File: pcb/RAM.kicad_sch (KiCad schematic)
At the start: 29 parts, among them U2 MT41K64M16TW-x

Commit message: Fix some symbols
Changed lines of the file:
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@@
   )
   (bus_alias "DQ_{L}" (members "DQ0" "DQ1" "DQ2" "DQ3" "DQ4" "DQ5" "DQ6" "DQ7" "LDM" "LDQS+" "LDQS-"))
-  (bus_alias "RAMCTRL" (members "ODT" "CKE" "CK+" "CK-" "~{MEM_RESET}" "~{CS}" "~{CAS}" "~{RAS}" "~{WE}"))
   (bus_alias "DQ_{U}" (members "DQ8" "DQ9" "DQ10" "DQ11" "DQ12" "DQ13" "DQ14" "DQ15" "UDM" "UDQS+" "UDQS-"))
   (bus_alias "RAMADDR" (members "A0" "A1" "A2" "A3" "A4" "A5" "A6" "A7" "A8" "A9" "A10" "A11" "A12" "BA0" "BA1" "BA2"))
+  (bus_alias "RAMCTRL" (members "ODT" "CKE" "CK+" "CK-" "~{MEM_RESET}" "~{CS}" "~{CAS}" "~{RAS}" "~{WE}"))
   (junction (at 158.75 38.1) (diameter 0) (color 0 0 0 0)
   )
@@
     (pin "2")
   )
-  (symbol (lib_name "RAM_VDD_2") (lib_id "ecp5u85-bse-usb:RAM_VDD") (at 86.36 24.13 0) (unit 1)
+  (symbol (lib_id "ecp5u85-bse-usb:RAM_VDD") (at 86.36 24.13 0) (unit 1)
     (in_bom yes) (on_board yes) (fields_autoplaced)
     (property "Reference" "#PWR0116" (id 0) (at 86.36 27.94 0)
@@
     (pin "1")
   )
+  (symbol (lib_id "power:PWR_FLAG") (at 144.78 27.94 0) (unit 1)
+    (in_bom yes) (on_board yes) (fields_autoplaced)
+    (property "Reference" "#FLG0102" (id 0) (at 144.78 26.035 0)
+      (effects (font (size 1.27 1.27)) hide)
+    )
+    (property "Value" "PWR_FLAG" (id 1) (at 144.78 22.86 0))
+    (property "Footprint" "" (id 2) (at 144.78 27.94 0)
+      (effects (font (size 1.27 1.27)) hide)
+    )
+    (property "Datasheet" "~" (id 3) (at 144.78 27.94 0)
+      (effects (font (size 1.27 1.27)) hide)
+    )
+    (pin "1")
+  )
   (symbol (lib_id "power:GND") (at 217.17 50.8 0) (mirror y) (unit 1)
     (in_bom yes) (on_board yes) (fields_autoplaced)
@@
     (pin "2")
   )
-  (symbol (lib_name "RAM_VDD_1") (lib_id "ecp5u85-bse-usb:RAM_VDD") (at 234.95 29.21 0) (unit 1)
+  (symbol (lib_id "ecp5u85-bse-usb:RAM_VDD") (at 234.95 29.21 0) (unit 1)
     (in_bom yes) (on_board yes) (fields_autoplaced)
     (property "Reference" "#PWR0112" (id 0) (at 234.95 33.02 0)
@@
     (pin "2")
   )
+  (symbol (lib_id "power:PWR_FLAG") (at 99.06 27.94 0) (unit 1)
+    (in_bom yes) (on_board yes) (fields_autoplaced)
+    (property "Reference" "#FLG0101" (id 0) (at 99.06 26.035 0)
+      (effects (font (size 1.27 1.27)) hide)
+    )
+    (property "Value" "PWR_FLAG" (id 1) (at 99.06 22.86 0))
+    (property "Footprint" "" (id 2) (at 99.06 27.94 0)
+      (effects (font (size 1.27 1.27)) hide)
+    )
+    (property "Datasheet" "~" (id 3) (at 99.06 27.94 0)
+      (effects (font (size 1.27 1.27)) hide)
+    )
+    (pin "1")
+  )
   (symbol (lib_id "Device:C") (at 73.66 44.45 0) (unit 1)

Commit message: Some extra fixes and notes
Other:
- note added: "We might need care with these chokes RAM can require 200-300mA at some moments"
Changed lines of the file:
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@@
   )
   (bus_alias "DQ_{L}" (members "DQ0" "DQ1" "DQ2" "DQ3" "DQ4" "DQ5" "DQ6" "DQ7" "LDM" "LDQS+" "LDQS-"))
+  (bus_alias "RAMADDR" (members "A0" "A1" "A2" "A3" "A4" "A5" "A6" "A7" "A8" "A9" "A10" "A11" "A12" "BA0" "BA1" "BA2"))
   (bus_alias "DQ_{U}" (members "DQ8" "DQ9" "DQ10" "DQ11" "DQ12" "DQ13" "DQ14" "DQ15" "UDM" "UDQS+" "UDQS-"))
   (bus_alias "RAMCTRL" (members "ODT" "CKE" "CK+" "CK-" "~{MEM_RESET}" "~{CS}" "~{CAS}" "~{RAS}" "~{WE}"))
-  (bus_alias "RAMADDR" (members "A0" "A1" "A2" "A3" "A4" "A5" "A6" "A7" "A8" "A9" "A10" "A11" "A12" "BA0" "BA1" "BA2"))
   (junction (at 158.75 38.1) (diameter 0) (color 0 0 0 0)
   )
@@
     (stroke (width 0) (type default) (color 0 0 0 0))
   )
+  (text "We might need care with these chokes\nRAM can require 200-300mA at some moments"
+    (at 139.065 19.685 0)
+    (effects (font (size 1.27 1.27)) (justify right bottom))
+  )
   (text "NB: Caps near DDR3 chip" (at 245.11 64.77 0)

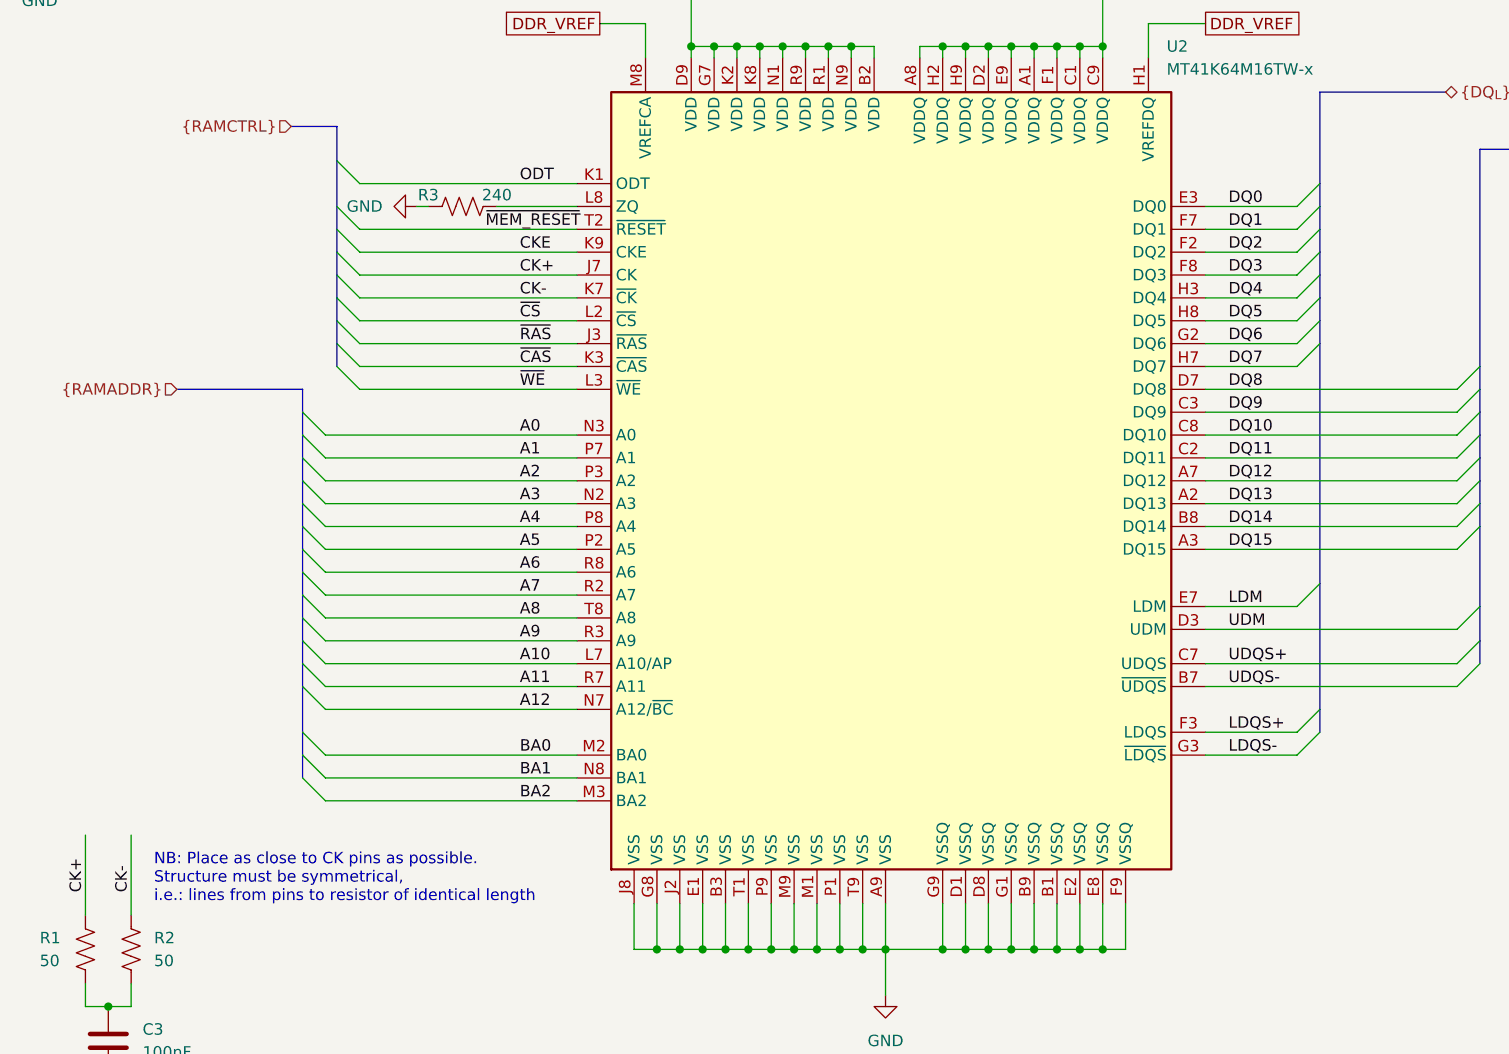
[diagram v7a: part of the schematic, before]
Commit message: Rename RAM nets to include prefix
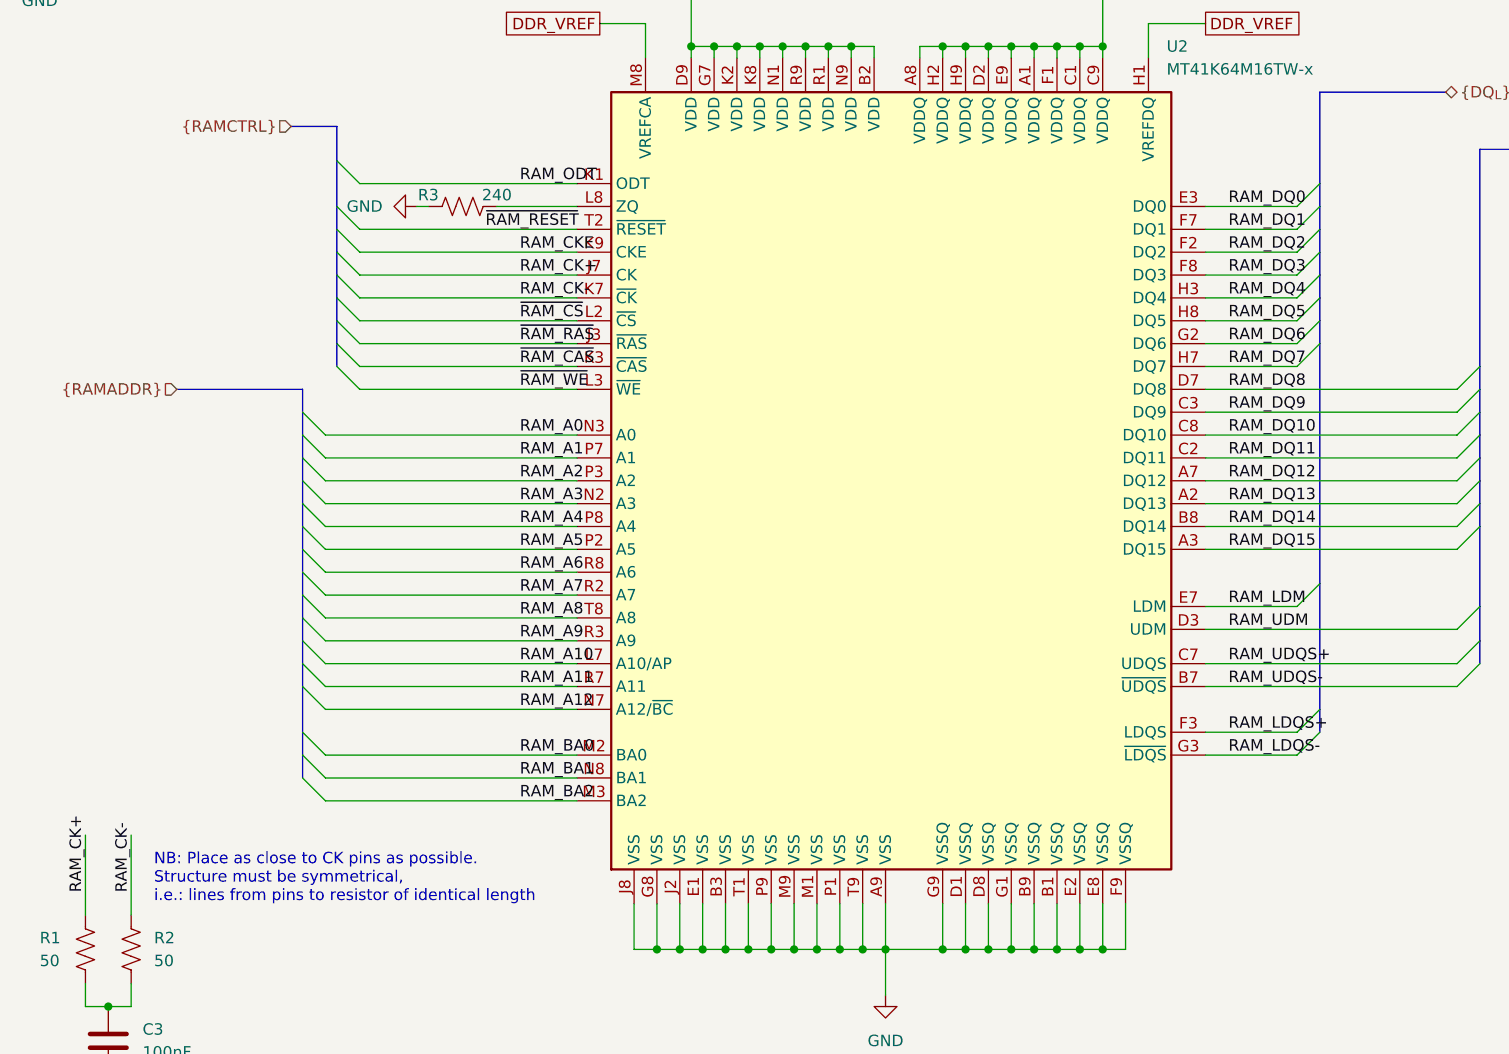
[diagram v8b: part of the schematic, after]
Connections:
- net A0 renamed RAM_A0
- net A1 renamed RAM_A1
- net A10 renamed RAM_A10
- net A11 renamed RAM_A11
- net A12 renamed RAM_A12
- net A2 renamed RAM_A2
- net A3 renamed RAM_A3
- net A4 renamed RAM_A4
- net A5 renamed RAM_A5
- net A6 renamed RAM_A6
- net A7 renamed RAM_A7
- net A8 renamed RAM_A8
- net A9 renamed RAM_A9
- net BA0 renamed RAM_BA0
- net BA1 renamed RAM_BA1
- net BA2 renamed RAM_BA2
- net CK+ renamed RAM_CK+
- net CK- renamed RAM_CK-
- net CKE renamed RAM_CKE
- net DQ0 renamed RAM_DQ0
- net DQ1 renamed RAM_DQ1
- net DQ10 renamed RAM_DQ10
- net DQ11 renamed RAM_DQ11
- net DQ12 renamed RAM_DQ12
- net DQ13 renamed RAM_DQ13
- net DQ14 renamed RAM_DQ14
- net DQ15 renamed RAM_DQ15
- net DQ2 renamed RAM_DQ2
- net DQ3 renamed RAM_DQ3
- net DQ4 renamed RAM_DQ4
- net DQ5 renamed RAM_DQ5
- net DQ6 renamed RAM_DQ6
- net DQ7 renamed RAM_DQ7
- net DQ8 renamed RAM_DQ8
- net DQ9 renamed RAM_DQ9
- net LDM renamed RAM_LDM
- net LDQS+ renamed RAM_LDQS+
- net LDQS- renamed RAM_LDQS-
- net ODT renamed RAM_ODT
- net UDM renamed RAM_UDM
- net UDQS+ renamed RAM_UDQS+
- net UDQS- renamed RAM_UDQS-
- net ~{CAS} renamed ~{RAM_CAS}
- net ~{CS} renamed ~{RAM_CS}
- net ~{MEM_RESET} renamed ~{RAM_RESET}
- net ~{RAS} renamed ~{RAM_RAS}
- net ~{WE} renamed ~{RAM_WE}
